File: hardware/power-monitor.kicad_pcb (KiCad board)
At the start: 2 copper layers, 50 x 60 mm, 27 parts, among them J2 Conn_01x04, J3 Screw_Terminal_01x02, J4 Screw_Terminal_01x02, SW1 RESET, U1 INA228, U2 ESP32-C3-WROOM-02, U3 SY8303

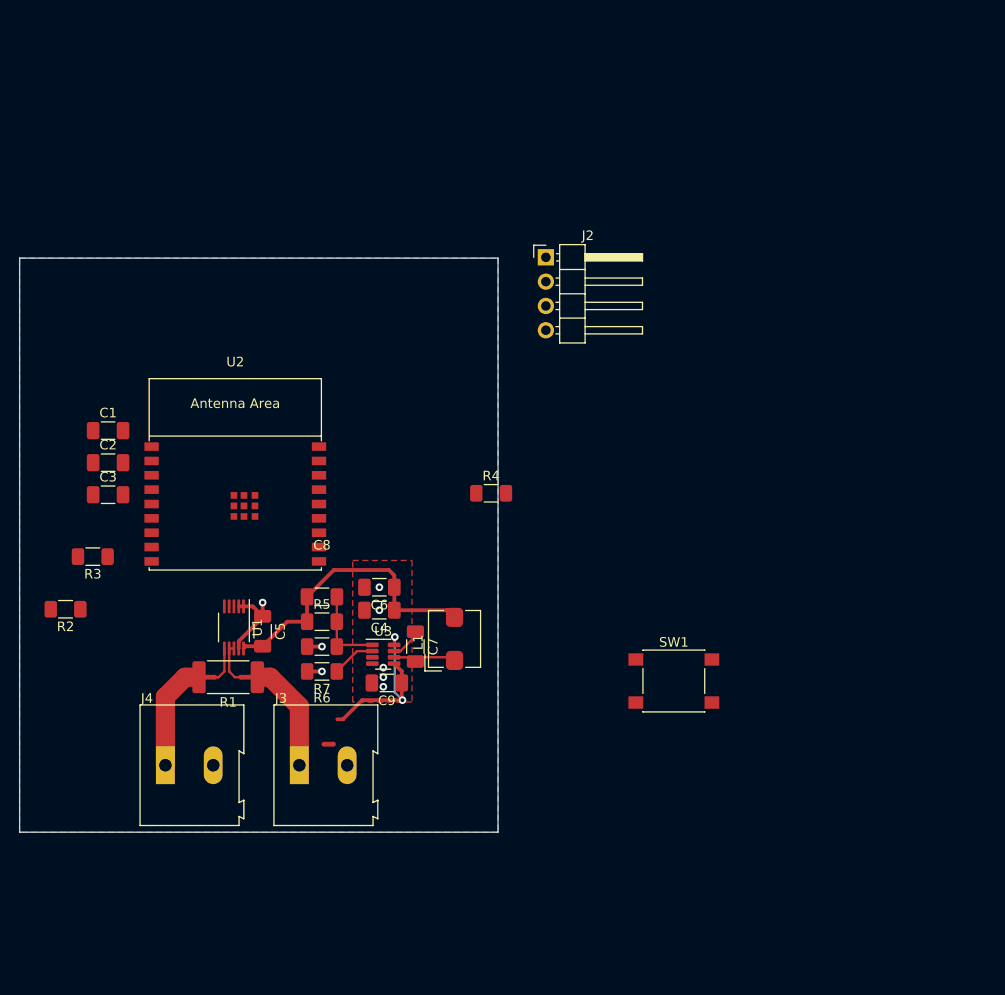
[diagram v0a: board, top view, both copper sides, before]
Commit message: PLC based hardware design
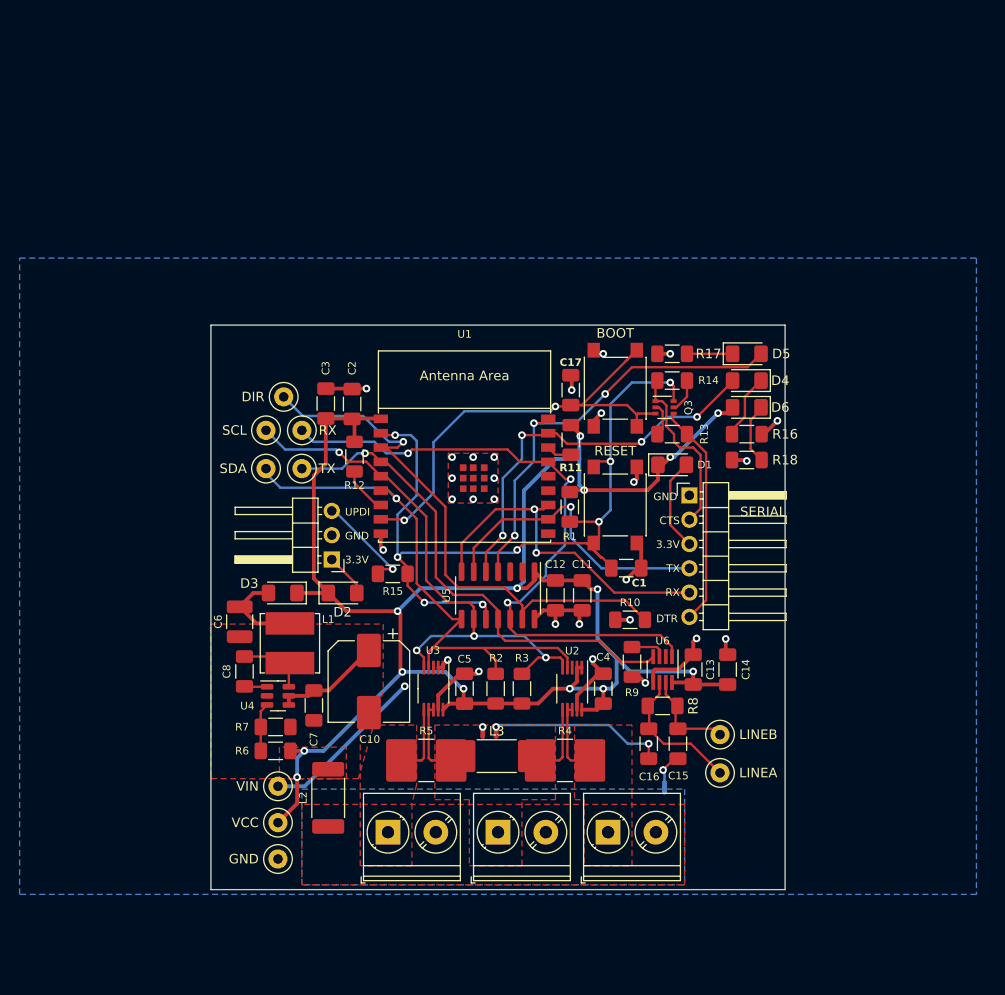
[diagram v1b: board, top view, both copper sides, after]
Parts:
- removed C9: C, Capacitor_SMD:C_1206_3216Metric_Pad1.33x1.80mm_HandSolder
- added C10: 22uF, Capacitor_SMD:CP_Elec_8x10, F.Cu at (136.5, 94.2)
- added C11: 1-10nF, Capacitor_SMD:C_1206_3216Metric_Pad1.33x1.80mm_HandSolder, F.Cu at (158.8, 85.2)
- added C12: 0.1uF, Capacitor_SMD:C_1206_3216Metric_Pad1.33x1.80mm_HandSolder, F.Cu at (156.0, 85.2)
- added C13: 1uF, Capacitor_SMD:C_1206_3216Metric_Pad1.33x1.80mm_HandSolder, F.Cu at (170.4, 93.0)
- added C14: 0.1uF, Capacitor_SMD:C_1206_3216Metric_Pad1.33x1.80mm_HandSolder, F.Cu at (174.0, 93.0)
- added C15: C_Small, Capacitor_SMD:C_1206_3216Metric_Pad1.33x1.80mm_HandSolder, F.Cu at (168.8, 100.8)
- added C16: C_Small, Capacitor_SMD:C_1206_3216Metric_Pad1.33x1.80mm_HandSolder, F.Cu at (165.8, 100.8)
- added C17: 10uF, Capacitor_SMD:C_1206_3216Metric_Pad1.33x1.80mm_HandSolder, F.Cu at (157.6, 63.8)
- added D1: D_Schottky, Diode_SMD:D_1206_3216Metric_Pad1.42x1.75mm_HandSolder, F.Cu at (168.2, 71.6)
- added D2: D_Schottky, Diode_SMD:D_1206_3216Metric_Pad1.42x1.75mm_HandSolder, F.Cu at (133.8, 85.0)
- added D3: D_Schottky, Diode_SMD:D_1206_3216Metric_Pad1.42x1.75mm_HandSolder, F.Cu at (127.5, 85.0)
- added D4: LED, LED_SMD:LED_1206_3216Metric_Pad1.42x1.75mm_HandSolder, F.Cu at (176.0, 62.8)
- added D5: LED, LED_SMD:LED_1206_3216Metric_Pad1.42x1.75mm_HandSolder, F.Cu at (176.0, 60.0)
- added D6: LED, LED_SMD:LED_1206_3216Metric_Pad1.42x1.75mm_HandSolder, F.Cu at (176.0, 65.6)
- added J1: Screw_Terminal_01x02, TerminalBlock_Phoenix:TerminalBlock_Phoenix_PT-1,5-2-5.0-H_1x02_P5.00mm_Horizontal, F.Cu at (138.5, 110.0)
- added J5: Conn_01x06, Connector_PinHeader_2.54mm:PinHeader_1x06_P2.54mm_Horizontal, F.Cu at (170.0, 74.8)
- added L2: L, Inductor_SMD:L_2512_6332Metric_Pad1.52x3.35mm_HandSolder, F.Cu at (132.2, 106.4)
- added L3: L, Inductor_SMD:L_2512_6332Metric_Pad1.52x3.35mm_HandSolder, F.Cu at (149.9, 102.0)
- added NT2: NetTie_2, hardware:NetTie-2_SMD_Pad0.25mm, F.Cu at (157.6, 102.5)
- added NT5: NetTie_2, hardware:NetTie-2_SMD_Pad0.25mm, F.Cu at (141.9, 102.5)
- added NT6: NetTie_2, NetTie:NetTie-2_SMD_Pad0.5mm, F.Cu at (149.8, 99.5)
- added NT7: NetTie_2, NetTie:NetTie-2_SMD_Pad0.5mm, B.Cu at (167.4, 105.3)
- added Q3: BC846BS, Package_TO_SOT_SMD:SOT-363_SC-70-6, F.Cu at (167.4, 65.6)
- added R10: 10k, Resistor_SMD:R_1206_3216Metric_Pad1.30x1.75mm_HandSolder, F.Cu at (163.8, 87.8)
- added R11: 10k, Resistor_SMD:R_1206_3216Metric_Pad1.30x1.75mm_HandSolder, F.Cu at (157.6, 69.0)
- added R12: 10k, Resistor_SMD:R_1206_3216Metric_Pad1.30x1.75mm_HandSolder, F.Cu at (135.0, 70.8)
- added R13: 10k, Resistor_SMD:R_1206_3216Metric_Pad1.30x1.75mm_HandSolder, F.Cu at (168.2, 68.4)
- added R14: 10k, Resistor_SMD:R_1206_3216Metric_Pad1.30x1.75mm_HandSolder, F.Cu at (168.2, 62.8)
- added R15: 470, Resistor_SMD:R_1206_3216Metric_Pad1.30x1.75mm_HandSolder, F.Cu at (139.0, 83.0)
- added R16: R, Resistor_SMD:R_1206_3216Metric_Pad1.30x1.75mm_HandSolder, F.Cu at (176.0, 68.4)
- added R17: R, Resistor_SMD:R_1206_3216Metric_Pad1.30x1.75mm_HandSolder, F.Cu at (168.2, 60.0)
- added R18: R, Resistor_SMD:R_1206_3216Metric_Pad1.30x1.75mm_HandSolder, F.Cu at (176.0, 71.1)
- added R8: 60, Resistor_SMD:R_1206_3216Metric_Pad1.30x1.75mm_HandSolder, F.Cu at (167.2, 96.8)
- added R9: 9.3k, Resistor_SMD:R_1206_3216Metric_Pad1.30x1.75mm_HandSolder, F.Cu at (164.0, 92.2)
- added SW2: BOOT, Button_Switch_SMD:SW_Push_1P1T_NO_6x6mm_H9.5mm, F.Cu at (162.2, 63.6)
- added TP1: SCL, TestPoint:TestPoint_Loop_D2.50mm_Drill1.0mm, F.Cu at (125.8, 68.0)
- added TP10: GND, TestPoint:TestPoint_Loop_D2.50mm_Drill1.0mm, F.Cu at (127.0, 112.8)
- added TP2: SDA, TestPoint:TestPoint_Loop_D2.50mm_Drill1.0mm, F.Cu at (125.8, 72.0)
- added TP3: RX, TestPoint:TestPoint_Loop_D2.50mm_Drill1.0mm, F.Cu at (129.5, 68.0)
- added TP4: TX, TestPoint:TestPoint_Loop_D2.50mm_Drill1.0mm, F.Cu at (129.5, 72.0)
- added TP5: DIR, TestPoint:TestPoint_Loop_D2.50mm_Drill1.0mm, F.Cu at (127.6, 64.5)
- added TP6: LINEB, TestPoint:TestPoint_Loop_D2.50mm_Drill1.0mm, F.Cu at (173.2, 99.8)
- added TP7: LINEA, TestPoint:TestPoint_Loop_D2.50mm_Drill1.0mm, F.Cu at (173.2, 103.8)
- added TP8: VIN, TestPoint:TestPoint_Loop_D2.50mm_Drill1.0mm, F.Cu at (127.0, 105.2)
- added TP9: VCC, TestPoint:TestPoint_Loop_D2.50mm_Drill1.0mm, F.Cu at (127.0, 109.0)
- added U4: LMR51610XDBVR, Package_TO_SOT_SMD:SOT-23-6, F.Cu at (127.0, 95.8)
- added U5: ATtiny424-SS, Package_SO:SOIC-14_3.9x8.7mm_P1.27mm, F.Cu at (150.0, 85.2)
- added U6: THVD8000, Package_TO_SOT_SMD:SOT-23-8_Handsoldering, F.Cu at (167.2, 93.0)
- C1: value 10uF -> 1uF
- C2: value 0.1uF -> 10uF
- C3: value 1uF -> 0.1uF
- C4: value C -> 0.1uF
- C6: value C -> 22uF / 16V; footprint Capacitor_SMD:C_1206_3216Metric_Pad1.33x1.80mm_HandSolder -> Capacitor_SMD:C_1210_3225Metric_Pad1.33x2.70mm_HandSolder
- C7: value C_Small -> 2.2uF
- C8: value C -> 0.1uF / 16V
- J2: value Conn_01x04 -> Screw_Terminal_01x02; footprint Connector_PinHeader_2.54mm:PinHeader_1x04_P2.54mm_Horizontal -> TerminalBlock_Phoenix:TerminalBlock_Phoenix_PT-1,5-2-5.0-H_1x02_P5.00mm_Horizontal
- J3: footprint TerminalBlock:TerminalBlock_Altech_AK300-2_P5.00mm -> TerminalBlock_Phoenix:TerminalBlock_Phoenix_PT-1,5-2-5.0-H_1x02_P5.00mm_Horizontal
- J4: value Screw_Terminal_01x02 -> Conn_01x03; footprint TerminalBlock:TerminalBlock_Altech_AK300-2_P5.00mm -> Connector_PinHeader_2.54mm:PinHeader_1x03_P2.54mm_Horizontal
- L1: value L -> 22 uH; footprint Inductor_SMD:L_Bourns_SRP5030T -> Inductor_SMD:L_Bourns_SRN6045TA
- NT3, NT4: footprint NetTie:NetTie-2_SMD_Pad0.5mm -> hardware:NetTie-2_SMD_Pad0.25mm
- R1: value 2mOhm -> 10k; footprint Resistor_SMD:R_2512_6332Metric_Pad1.40x3.35mm_HandSolder -> Resistor_SMD:R_1206_3216Metric_Pad1.30x1.75mm_HandSolder
- R4: value 10k -> 2mOhm; footprint Resistor_SMD:R_1206_3216Metric_Pad1.30x1.75mm_HandSolder -> Resistor_SMD:R_2816_7142Metric_Pad3.20x4.45mm_HandSolder
- R5: value R -> 2mOhm; footprint Resistor_SMD:R_1206_3216Metric_Pad1.30x1.75mm_HandSolder -> Resistor_SMD:R_2816_7142Metric_Pad3.20x4.45mm_HandSolder
- R6: value R -> 69.8k
- R7: value R -> 22.1k
- U1: value INA228 -> ESP32-C3-WROOM-02; footprint Package_SO:VSSOP-10_3x3mm_P0.5mm -> PCM_Espressif:ESP32-C3-WROOM-02
- U2: value ESP32-C3-WROOM-02 -> INA228; footprint PCM_Espressif:ESP32-C3-WROOM-02 -> Package_SO:VSSOP-10_3x3mm_P0.5mm
- U3: value SY8303 -> INA228; footprint Package_TO_SOT_SMD:SOT-23-8 -> Package_SO:VSSOP-10_3x3mm_P0.5mm
- moved J2 60.4 mm to (161.5, 110.0)
- moved C1 56.0 mm to (163.4, 82.4)
- moved R3 46.9 mm to (152.5, 95.0), turned to 90 degrees
- moved R2 45.7 mm to (149.8, 95.0), turned to 90 degrees
- moved U2 40.2 mm to (157.8, 95.0), turned to -90 degrees
- moved R1 39.9 mm to (157.5, 76.0), turned to -90 degrees
- moved NT3 33.9 mm to (156.4, 102.5), turned to 0 degrees
- moved NT1 29.1 mm to (148.4, 99.5), turned to 90 degrees
- moved R4 29.0 mm to (157.0, 102.5), turned to 180 degrees
- moved U1 28.9 mm to (146.5, 72.7), turned to 0 degrees
- moved J4 27.7 mm to (132.6, 81.5), turned to 180 degrees
- moved C2 26.2 mm to (134.8, 65.2), turned to 90 degrees
- moved C4 24.8 mm to (161.0, 95.0), turned to -90 degrees
- moved C3 24.7 mm to (132.0, 65.2), turned to 90 degrees
- moved C5 21.9 mm to (146.5, 95.0)
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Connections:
- C1 pad 1: VCC -> /ATTiny/RESET
- C3 pad 1: /EN -> VCC
- C4 pad 1: VCC -> GND
- C4 pad 2: GND -> VCC
- C6 pad 1: VCC -> /Supply/OUTPUT
- C7 pad 1: Net-(U3-BS) -> Net-(U4-EN)
- C7 pad 2: Net-(U3-LX) -> GND
- C8 pad 1: VCC -> Net-(U4-CB)
- C8 pad 2: Net-(U3-FB) -> Net-(U4-SW)
- J2 pad 1: VCC -> /Sense2/INA
- J2 pad 2: /RX -> /VNEG
- J3 pad 1: /Vpanel -> /VNEG
- J3 pad 2: GND -> /VNEG
- J4 pad 1: /Vout -> Net-(D2-A)
- L1 pad 1: Net-(U3-LX) -> Net-(U4-SW)
- L1 pad 2: VCC -> /Supply/OUTPUT
- NT1 pad 1: /Vout -> /VNEG
- NT1 pad 2: Net-(U1-IN+) -> /Supply/INPUT
- NT3 pad 1: /Vpanel -> /VNEG
- NT3 pad 2: Net-(U1-IN-) -> Net-(U2-IN+)
- NT4 pad 1: /Vpanel -> /VNEG
- NT4 pad 2: /VIN -> Net-(U3-IN-)
- R1 pad 1: /Vpanel -> VCC
- R1 pad 2: /Vout -> /ATTiny/RESET
- R2 pad 2: /SCL -> /ATTiny/SDA
- R3 pad 2: /SDA -> /ATTiny/SCL
- R4 pad 1: VCC -> /Sense2/INA
- R4 pad 2: /EN -> /VNEG
- R5 pad 1: VCC -> /VNEG
- R5 pad 2: Net-(U3-FB) -> /Sense1/INB
- R6 pad 1: Net-(U3-FB) -> VCC
- R6 pad 2: GND -> Net-(U4-FB)
- R7 pad 1: Net-(U3-FS) -> Net-(U4-FB)
- SW1 pad 1: GND -> /ATTiny/RESET
- SW1 pad 2: /EN -> GND
- U1 pad 1: GND -> VCC
- U1 pad 10: VCC -> unconnected-(U1-GPIO10-Pad10)
- U1 pad 2: GND -> /ATTiny/RESET
- U1 pad 3: unconnected-(U1-ALERT-Pad3) -> /ATTiny/PLC_DIR
- U1 pad 4: /SDA -> /ATTiny/PLC_TX
- U1 pad 5: /SCL -> /ATTiny/SCL
- U1 pad 6: Net-(U1-IN+) -> /ATTiny/SDA
- U1 pad 7: Net-(U1-IN-) -> Net-(U1-GPIO8)
- U1 pad 8: Net-(U1-IN-) -> /ESP32/BOOT
- U2 pad 10: unconnected-(U2-GPIO10-Pad10) -> VCC
- U2 pad 2: /EN -> VCC
- U2 pad 4: unconnected-(U2-GPIO5/ADC2_CH0-Pad4) -> /ATTiny/SDA
- U2 pad 5: unconnected-(U2-GPIO6-Pad5) -> /ATTiny/SCL
- U2 pad 6: /SDA -> Net-(U2-IN+)
- U2 pad 7: /SCL -> Net-(U2-IN-)
- U2 pad 8: unconnected-(U2-GPIO9-Pad8) -> Net-(U2-IN-)
- U3 pad 1: Net-(U3-FB) -> GND
- U3 pad 2: Net-(U3-FS) -> GND
- U3 pad 3: GND -> unconnected-(U3-ALERT-Pad3)
- U3 pad 4: GND -> /ATTiny/SDA
- U3 pad 5: /VIN -> /ATTiny/SCL
- U3 pad 6: Net-(U3-LX) -> Net-(U3-IN+)
- U3 pad 7: Net-(U3-BS) -> Net-(U3-IN-)
- U3 pad 8: /VIN -> Net-(U3-IN-)
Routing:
- net VCC: track 31.2 -> 204.1 mm, vias 0 -> 14
- net /ATTiny/RESET: track 0.00 -> 86.3 mm, vias 0 -> 8
- net /ATTiny/PLC_RX: track 0.00 -> 68.4 mm, vias 0 -> 3
- net /ATTiny/SCL: track 0.00 -> 59.4 mm, vias 0 -> 4
- net /ATTiny/PLC_DIR: track 0.00 -> 59.2 mm, vias 0 -> 1
- net /ATTiny/SDA: track 0.00 -> 59.0 mm, vias 0 -> 1
- net /ATTiny/PLC_TX: track 0.00 -> 52.1 mm, vias 0 -> 1
- net /ESP32/BOOT: track 0.00 -> 49.9 mm, vias 0 -> 2
- net GND: track 11.9 -> 59.5 mm, vias 8 -> 27
- net /ATTiny/LED1: track 0.00 -> 45.5 mm, vias 0 -> 3
- net /ATTiny/LED2: track 0.00 -> 41.2 mm, vias 0 -> 4
- net /RX: track 0.00 -> 36.0 mm, vias 0 -> 2
- net /TX: track 0.00 -> 31.3 mm, vias 0 -> 1
- net Net-(U4-EN): track 0.00 -> 29.7 mm, vias 0 -> 1
- net /DTR: track 0.00 -> 23.5 mm
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- added copper zone on F.Cu, net /Sense1/INB
- added copper zone on F.Cu, net /Sense2/INA
- added copper zone on B.Cu, net /VNEG
- added copper zone on F.Cu, net /VNEG
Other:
- board size 50 x 60 mm -> 60 x 59 mm
- board text added: "3.3V"
- board text added: "CTS"
- board text added: "DTR"
- board text added: "GND"
- board text added: "RX"
- board text added: "SERIAL"
- board text added: "TX"
- board text added: "UPDI"

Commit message: Remove PLC, use ESP
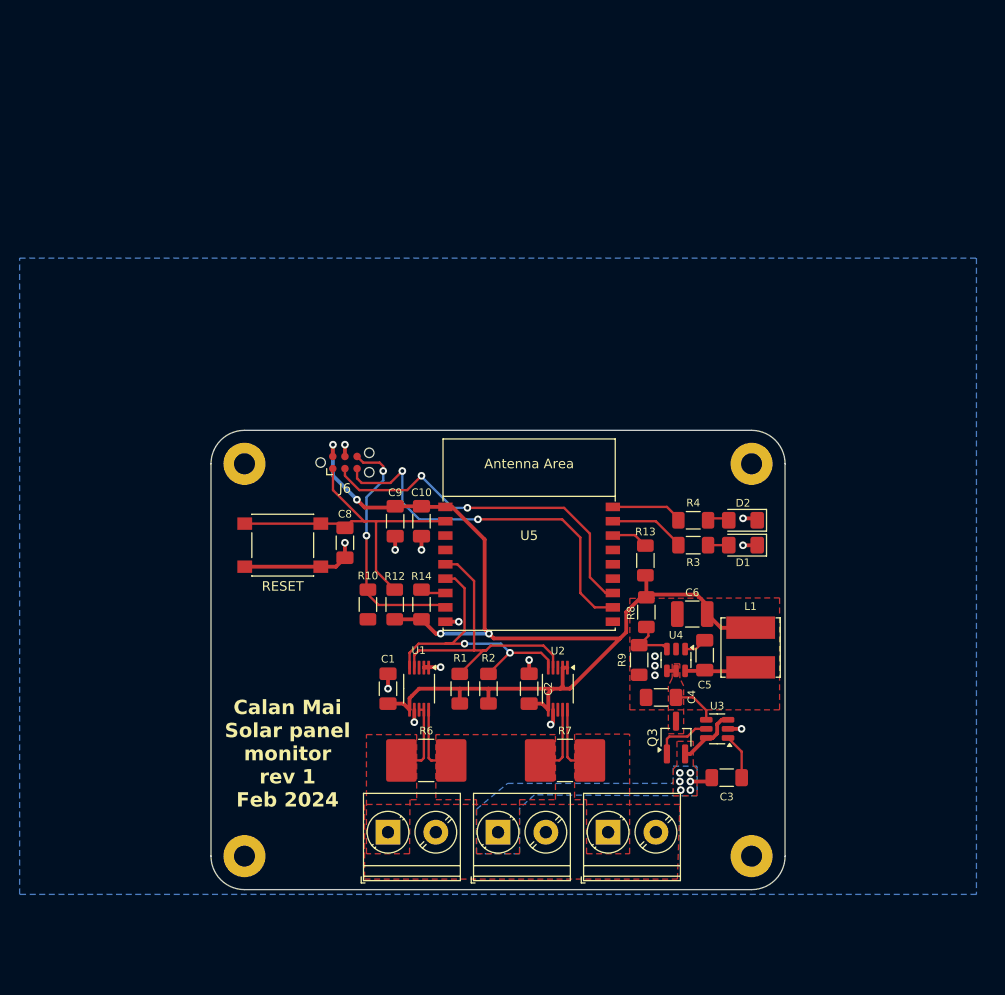
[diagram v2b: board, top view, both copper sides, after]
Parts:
- removed the C1 at (163.4, 82.4)
- removed C11: 1-10nF, Capacitor_SMD:C_1206_3216Metric_Pad1.33x1.80mm_HandSolder
- removed C12, C14: 0.1uF, Capacitor_SMD:C_1206_3216Metric_Pad1.33x1.80mm_HandSolder
- removed C13: 1uF, Capacitor_SMD:C_1206_3216Metric_Pad1.33x1.80mm_HandSolder
- removed C15, C16: C_Small, Capacitor_SMD:C_1206_3216Metric_Pad1.33x1.80mm_HandSolder
- removed C17: 10uF, Capacitor_SMD:C_1206_3216Metric_Pad1.33x1.80mm_HandSolder
- removed the C2 at (134.8, 65.2)
- removed D3: D_Schottky, Diode_SMD:D_1206_3216Metric_Pad1.42x1.75mm_HandSolder
- removed D4, D5, D6: LED, LED_SMD:LED_1206_3216Metric_Pad1.42x1.75mm_HandSolder
- removed J4: Conn_01x03, Connector_PinHeader_2.54mm:PinHeader_1x03_P2.54mm_Horizontal
- removed J5: Conn_01x06, Connector_PinHeader_2.54mm:PinHeader_1x06_P2.54mm_Horizontal
- removed L2, L3: L, Inductor_SMD:L_2512_6332Metric_Pad1.52x3.35mm_HandSolder
- removed the NT1 at (148.4, 99.5)
- removed NT6, NT7: NetTie_2, NetTie:NetTie-2_SMD_Pad0.5mm
- removed the R1 at (157.5, 76.0)
- removed R11: 10k, Resistor_SMD:R_1206_3216Metric_Pad1.30x1.75mm_HandSolder
- removed R15: 470, Resistor_SMD:R_1206_3216Metric_Pad1.30x1.75mm_HandSolder
- removed R16, R17, R18: R, Resistor_SMD:R_1206_3216Metric_Pad1.30x1.75mm_HandSolder
- removed the R8 at (167.2, 96.8)
- removed the R9 at (164.0, 92.2)
- removed SW2: BOOT, Button_Switch_SMD:SW_Push_1P1T_NO_6x6mm_H9.5mm
- removed TP1: SCL, TestPoint:TestPoint_Loop_D2.50mm_Drill1.0mm
- removed TP10: GND, TestPoint:TestPoint_Loop_D2.50mm_Drill1.0mm
- removed TP2: SDA, TestPoint:TestPoint_Loop_D2.50mm_Drill1.0mm
- removed TP3: RX, TestPoint:TestPoint_Loop_D2.50mm_Drill1.0mm
- removed TP4: TX, TestPoint:TestPoint_Loop_D2.50mm_Drill1.0mm
- removed TP5: DIR, TestPoint:TestPoint_Loop_D2.50mm_Drill1.0mm
- removed TP6: LINEB, TestPoint:TestPoint_Loop_D2.50mm_Drill1.0mm
- removed TP7: LINEA, TestPoint:TestPoint_Loop_D2.50mm_Drill1.0mm
- removed TP8: VIN, TestPoint:TestPoint_Loop_D2.50mm_Drill1.0mm
- removed TP9: VCC, TestPoint:TestPoint_Loop_D2.50mm_Drill1.0mm
- removed the U1 at (146.5, 72.7)
- removed U6: THVD8000, Package_TO_SOT_SMD:SOT-23-8_Handsoldering
- added C8: C, Capacitor_SMD:C_1206_3216Metric_Pad1.33x1.80mm_HandSolder, F.Cu at (134.0, 79.8)
- added C9: 10uF, Capacitor_SMD:C_1206_3216Metric_Pad1.33x1.80mm_HandSolder, F.Cu at (139.2, 77.5)
- added H1: MountingHole_Pad, MountingHole:MountingHole_2.2mm_M2_Pad, F.Cu at (123.5, 71.5)
- added H2: MountingHole_Pad, MountingHole:MountingHole_2.2mm_M2_Pad, F.Cu at (176.5, 71.5)
- added H3: MountingHole_Pad, MountingHole:MountingHole_2.2mm_M2_Pad, F.Cu at (176.5, 112.5)
- added H4: MountingHole_Pad, MountingHole:MountingHole_2.2mm_M2_Pad, F.Cu at (123.5, 112.5)
- added J6: PROG, Connector:Tag-Connect_TC2030-IDC-NL_2x03_P1.27mm_Vertical, F.Cu at (134.0, 71.4)
- added R3: 1k, Resistor_SMD:R_1206_3216Metric_Pad1.30x1.75mm_HandSolder, F.Cu at (170.4, 80.0)
- added R4: 1k, Resistor_SMD:R_1206_3216Metric_Pad1.30x1.75mm_HandSolder, F.Cu at (170.4, 77.4)
- added U3: LM74700, Package_TO_SOT_SMD:SOT-23-6, F.Cu at (172.9, 99.2)
- C10: value 22uF -> 0.1uF; footprint Capacitor_SMD:CP_Elec_8x10 -> Capacitor_SMD:C_1206_3216Metric_Pad1.33x1.80mm_HandSolder
- C3: value 0.1uF -> C
- D1, D2: value D_Schottky -> LED; footprint Diode_SMD:D_1206_3216Metric_Pad1.42x1.75mm_HandSolder -> LED_SMD:LED_1206_3216Metric_Pad1.42x1.75mm_HandSolder
- NT1: renamed from NT4; footprint hardware:NetTie-2_SMD_Pad0.25mm -> footprints:NetTie-2_SMD_Pad0.25mm
- NT2: renamed from NT5; footprint hardware:NetTie-2_SMD_Pad0.25mm -> footprints:NetTie-2_SMD_Pad0.25mm
- NT3: renamed from NT2; footprint hardware:NetTie-2_SMD_Pad0.25mm -> footprints:NetTie-2_SMD_Pad0.25mm
- NT4: renamed from NT3; footprint hardware:NetTie-2_SMD_Pad0.25mm -> footprints:NetTie-2_SMD_Pad0.25mm
- Q3: value BC846BS -> Q_NMOS_GSD; footprint Package_TO_SOT_SMD:SOT-363_SC-70-6 -> Package_TO_SOT_SMD:TSOT-23_HandSoldering
- U5: value ATtiny424-SS -> ESP32-C3-WROOM-02-NOTHERMAL; footprint Package_SO:SOIC-14_3.9x8.7mm_P1.27mm -> footprints:ESP32-C3-WROOM-02-NOTHERMAL
- moved C3 57.3 mm to (173.9, 104.3), turned to 0 degrees
- moved L1 48.2 mm to (176.4, 90.7)
- moved C5 48.1 mm to (171.6, 91.5), turned to -90 degrees
- moved C6 47.3 mm to (170.3, 87.2), turned to 180 degrees
- moved D2 42.5 mm to (175.6, 77.4), turned to 180 degrees
- moved U4 41.8 mm to (168.6, 92.0), turned to -90 degrees
- moved R8 41.4 mm to (165.5, 87.0), turned to -90 degrees
- moved R9 38.6 mm to (164.8, 92.0), turned to -90 degrees
- moved C4 36.3 mm to (167.0, 95.9), turned to 180 degrees
- moved R14 35.1 mm to (142.0, 86.2), turned to -90 degrees
- moved SW3 35.0 mm to (127.5, 80.0), turned to 0 degrees
- moved Q3 34.5 mm to (168.6, 100.1), turned to 90 degrees
- moved R10 27.4 mm to (136.4, 86.2), turned to -90 degrees
- moved C10 17.6 mm to (142.0, 77.5)
- moved R12 16.0 mm to (139.2, 86.2)
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- renumbered C5 to C1, C4 to C2, C7 to C4, C8 to C5, R2 to R1, R3 to R2, R5 to R6, R4 to R7, R6 to R8, R7 to R9, SW1 to SW3, U3 to U1
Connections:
- net Net-(U4-CB) renamed /Supply/CB
- net Net-(U4-FB) renamed /Supply/FEEDBACK
- net Net-(U4-SW) renamed /Supply/SW
- C10 pad 1: Net-(U4-EN) -> VCC
- C3 pad 1: VCC -> Net-(D3-A2)
- C3 pad 2: GND -> Net-(U3-VCAP)
- C4 pad 1: Net-(U4-EN) -> Net-(Q3-D)
- C6 pad 1: /Supply/OUTPUT -> VCC
- D1 pad 1: VCC -> GND
- D2 pad 1: VCC -> GND
- J1 pad 2: /VNEG -> GND
- J2 pad 2: /VNEG -> GND
- J3 pad 1: /VNEG -> /VPOS
- J3 pad 2: /VNEG -> GND
- L1 pad 2: /Supply/OUTPUT -> VCC
- NT1 pad 1: /VNEG -> /VPOS
- NT1 pad 2: Net-(U3-IN-) -> Net-(U1-Vin+)
- NT2 pad 2: Net-(U3-IN+) -> Net-(U1-Vbus)
- NT3 pad 2: Net-(U2-IN-) -> Net-(U2-Vin+)
- NT4 pad 1: /VNEG -> /VPOS
- NT4 pad 2: Net-(U2-IN+) -> Net-(U2-Vbus)
- Q3 pad 1: /CTS -> Net-(Q3-G)
- Q3 pad 2: Net-(Q3A-B1) -> Net-(D3-A2)
- Q3 pad 3: /ESP32/BOOT -> Net-(Q3-D)
- R1 pad 2: /ATTiny/SDA -> /ESP32/SDA
- R10 pad 1: /ATTiny/PLC_DIR -> /ESP32/BOOT
- R10 pad 2: GND -> VCC
- R12 pad 1: Net-(U1-GPIO8) -> VCC
- R12 pad 2: VCC -> /ESP32/EN
- R13 pad 1: Net-(Q3A-B1) -> /ESP32/IO2
- R13 pad 2: /DTR -> VCC
- R14 pad 1: Net-(Q3B-B2) -> /ESP32/IO8
- R14 pad 2: /CTS -> VCC
- R2 pad 2: /ATTiny/SCL -> /ESP32/SCL
- R6 pad 1: /VNEG -> /VPOS
- R7 pad 2: /VNEG -> /VPOS
- SW3 pad 1: /ATTiny/RESET -> /ESP32/EN
- U1 pad 10: VCC -> Net-(U1-Vin+)
- U1 pad 4: /ATTiny/SDA -> /ESP32/SDA
- U1 pad 5: /ATTiny/SCL -> /ESP32/SCL
- U1 pad 6: Net-(U3-IN+) -> VCC
- U1 pad 7: Net-(U3-IN-) -> GND
- U1 pad 8: Net-(U3-IN-) -> Net-(U1-Vbus)
- U1 pad 9: GND -> Net-(U1-Vbus)
- U2 pad 10: VCC -> Net-(U2-Vin+)
- U2 pad 4: /ATTiny/SDA -> /ESP32/SDA
- U2 pad 5: /ATTiny/SCL -> /ESP32/SCL
- U2 pad 6: Net-(U2-IN+) -> VCC
- U2 pad 7: Net-(U2-IN-) -> GND
- U2 pad 8: Net-(U2-IN-) -> Net-(U2-Vbus)
- U2 pad 9: GND -> Net-(U2-Vbus)
- U4 pad 4: Net-(U4-EN) -> Net-(Q3-D)
- U4 pad 5: Net-(U4-EN) -> Net-(Q3-D)
- U5 pad 10: /ATTiny/RESET -> unconnected-(U5-GPIO10-Pad10)
- U5 pad 11: /ATTiny/PLC_TX -> /ESP32/RXD
- U5 pad 12: /ATTiny/PLC_RX -> /ESP32/TXD
- U5 pad 13: /ATTiny/PLC_DIR -> unconnected-(U5-GPIO18/USB_D--Pad13)
- U5 pad 14: GND -> unconnected-(U5-GPIO19/USB_D+-Pad14)
- U5 pad 2: unconnected-(U5-PA4-Pad2) -> /ESP32/EN
- U5 pad 4: /ATTiny/LED1 -> unconnected-(U5-GPIO5/ADC2_CH0-Pad4)
- U5 pad 5: /ATTiny/LED2 -> /ESP32/SDA
- U5 pad 6: /TX -> /ESP32/SCL
- U5 pad 7: /RX -> /ESP32/IO8
- U5 pad 8: /ATTiny/SDA -> /ESP32/BOOT
- U5 pad 9: /ATTiny/SCL -> GND
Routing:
- net VCC: track 204.1 -> 115.6 mm, vias 14 -> 4
- net /ATTiny/RESET: track 86.3 -> 0.00 mm, vias 8 -> 0
- net /ATTiny/PLC_RX: track 68.4 -> 0.00 mm, vias 3 -> 0
- net /ATTiny/SCL: track 59.4 -> 0.00 mm, vias 4 -> 0
- net /ATTiny/PLC_DIR: track 59.2 -> 0.00 mm, vias 1 -> 0
- net /ATTiny/SDA: track 59.0 -> 0.00 mm, vias 1 -> 0
- net /ATTiny/PLC_TX: track 52.1 -> 0.00 mm, vias 1 -> 0
- net /ATTiny/LED1: track 45.5 -> 0.00 mm, vias 3 -> 0
- net /ATTiny/LED2: track 41.2 -> 0.00 mm, vias 4 -> 0
- net /ESP32/RXD: track 0.00 -> 39.7 mm, vias 0 -> 2
- net /ESP32/TXD: track 0.00 -> 37.8 mm, vias 0 -> 2
- net /RX: track 36.0 -> 0.00 mm, vias 2 -> 0
- net /ESP32/EN: track 0.00 -> 35.9 mm
- net /ESP32/SDA: track 0.00 -> 32.7 mm
- net /TX: track 31.3 -> 0.00 mm, vias 1 -> 0
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- added copper zone on B.Cu, net /VPOS
- added copper zone on F.Cu, net /VPOS
- added copper zone on F.Cu, net Net-(Q3-D)
- removed copper zone on B.Cu, net /VNEG
- removed copper zone on F.Cu, net /VNEG
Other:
- board size 60 x 59 mm -> 60 x 48 mm
- board text added: "Calan Mai Solar panel monitor rev 1 Feb 2024"
- board text removed: "3.3V"
- board text removed: "CTS"
- board text removed: "DTR"
- board text removed: "GND"
- board text removed: "RX"
- board text removed: "SERIAL"
- board text removed: "TX"
- board text removed: "UPDI"
